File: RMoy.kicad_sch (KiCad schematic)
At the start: 20 parts, among them J1 AudioJack3_SwitchTR, J2 AudioJack3_SwitchTR, J3 Jack-DC, U1 OPA2134

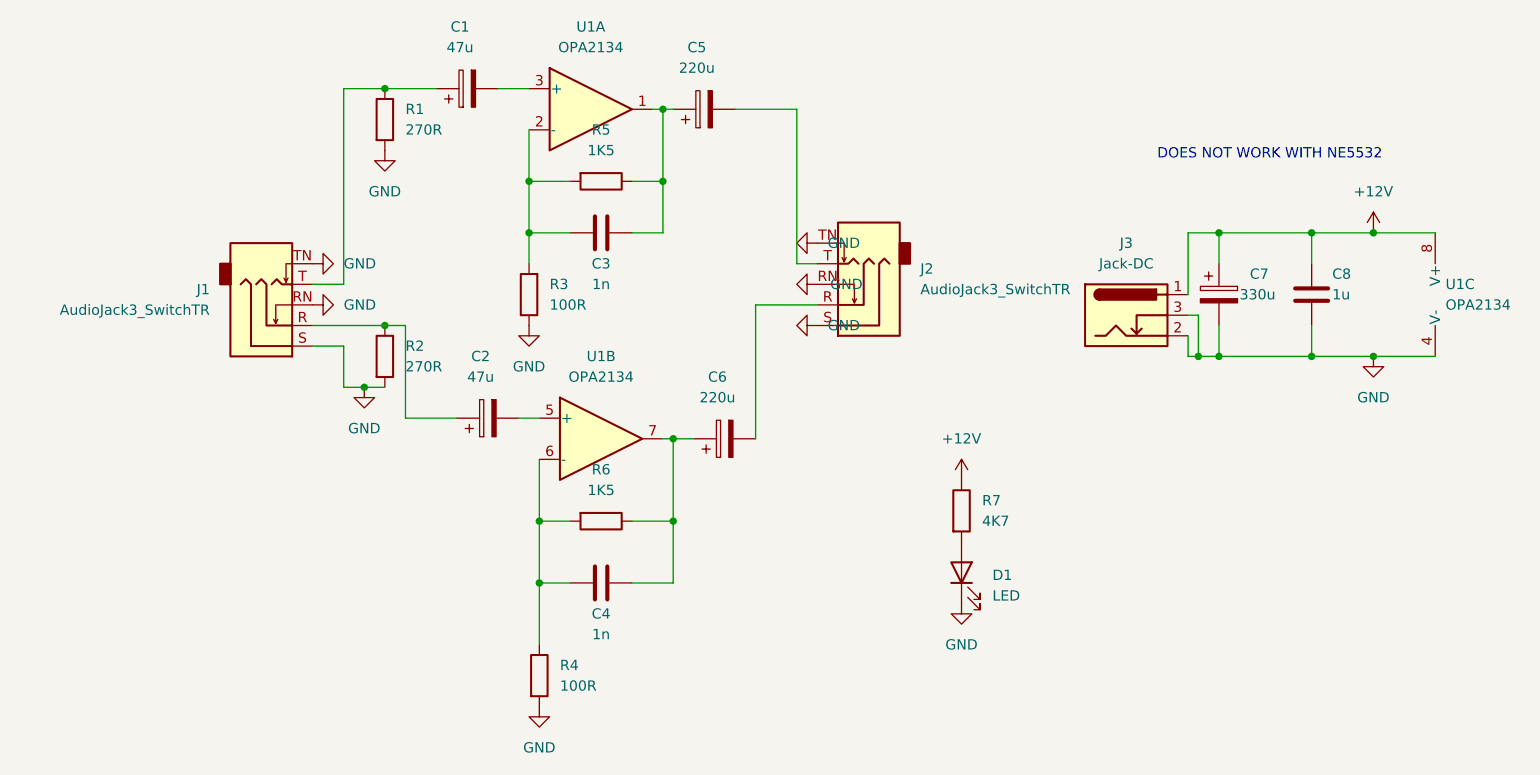
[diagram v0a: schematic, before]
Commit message: add revised parts list
TODO: C1/C2/C5/C6 have not been modified, are they obsolete?
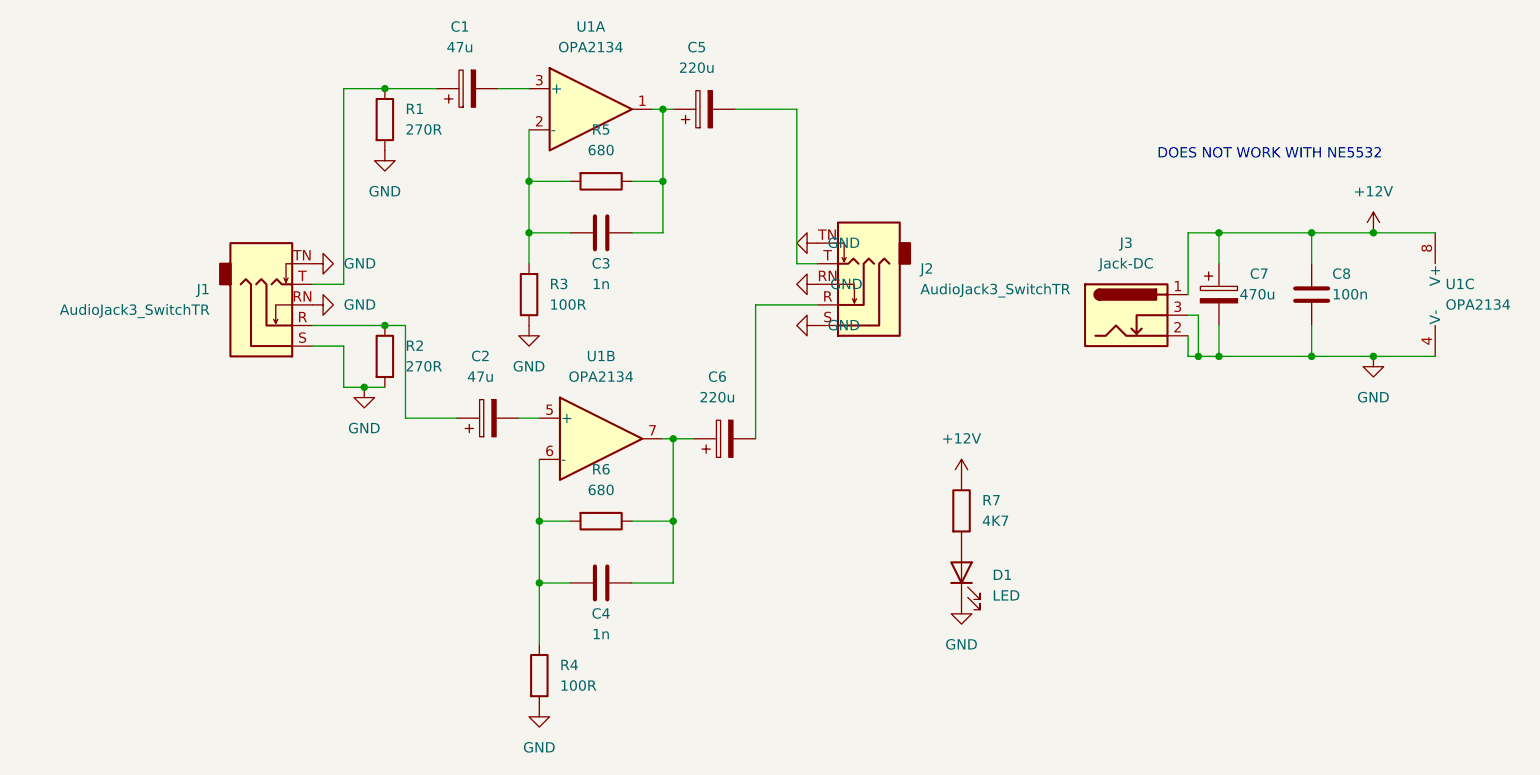
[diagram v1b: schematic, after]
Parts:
- C3, C4: footprint Capacitor_THT:C_Rect_L7.2mm_W2.5mm_P5.00mm_FKS2_FKP2_MKS2_MKP2 -> Capacitor_THT:C_Disc_D5.0mm_W2.5mm_P5.00mm
- C7: value 330u -> 470u
- C8: value 1u -> 100n; footprint Capacitor_THT:C_Rect_L4.6mm_W5.5mm_P2.50mm_MKS02_FKP02 -> Capacitor_THT:C_Disc_D5.0mm_W2.5mm_P5.00mm
- R5, R6: value 1K5 -> 680

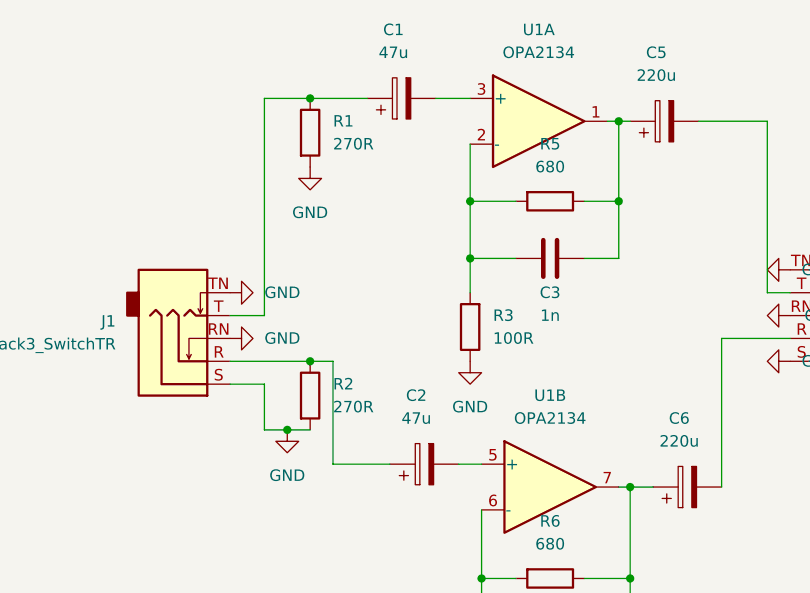
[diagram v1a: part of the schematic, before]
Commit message: C1/C2 are now 100µF non-EOL parts
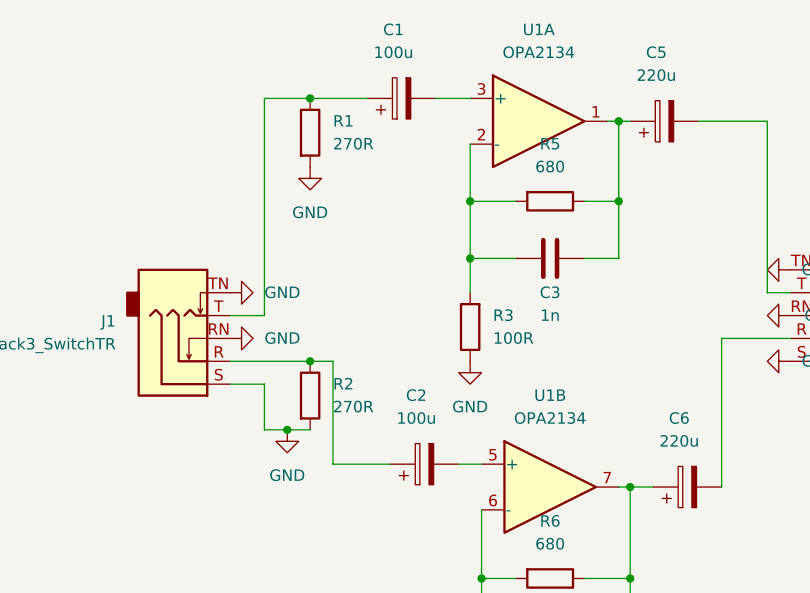
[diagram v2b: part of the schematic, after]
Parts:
- C1, C2: value 47u -> 100u; footprint Capacitor_THT:CP_Radial_D5.0mm_P2.00mm -> Capacitor_THT:CP_Radial_D8.0mm_P3.50mm
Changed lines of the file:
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@@
 			)
 		)
-		(property "Value" "47u"
+		(property "Value" "100u"
 			(at 66.421 67.31 90)
 			(effects
@@
 			)
 		)
-		(property "Footprint" "Capacitor_THT:CP_Radial_D5.0mm_P2.00mm"
+		(property "Footprint" "Capacitor_THT:CP_Radial_D8.0mm_P3.50mm"
 			(at 71.12 71.4248 0)
 			(effects
@@
 			)
 		)
-		(property "Value" "47u"
+		(property "Value" "100u"
 			(at 68.961 107.95 90)
 			(effects
@@
 			)
 		)
-		(property "Footprint" "Capacitor_THT:CP_Radial_D5.0mm_P2.00mm"
+		(property "Footprint" "Capacitor_THT:CP_Radial_D8.0mm_P3.50mm"
 			(at 73.66 112.0648 0)
 			(effects

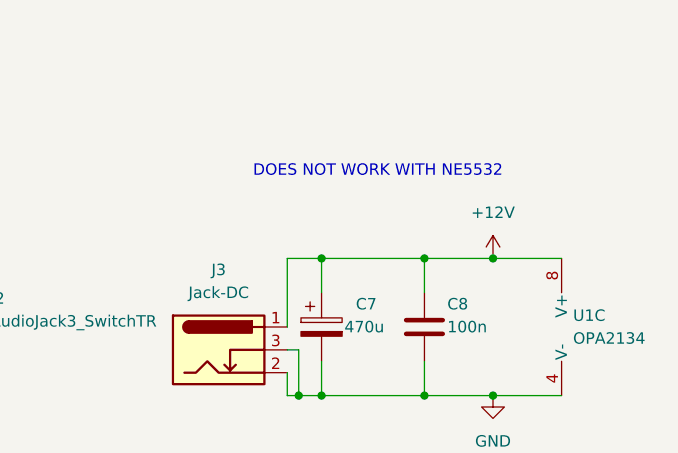
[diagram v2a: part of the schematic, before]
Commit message: PCB is reworked
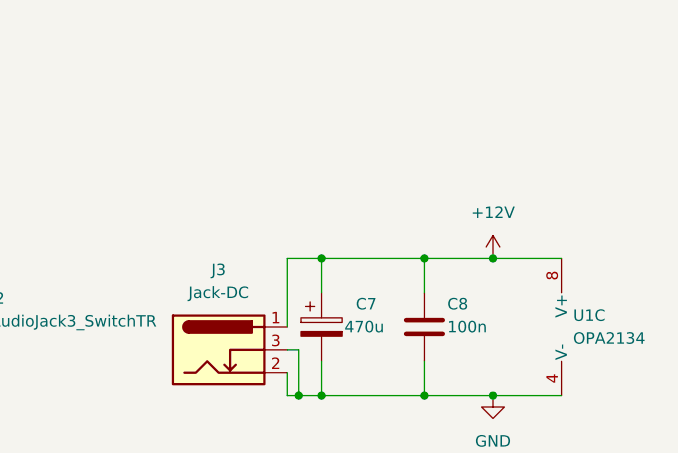
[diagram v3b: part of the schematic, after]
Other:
- note removed: "DOES NOT WORK WITH NE5532"
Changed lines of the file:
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@@
-		)
-	)
-	(text "DOES NOT WORK WITH NE5532"
-		(exclude_from_sim no)
-		(at 152.4 81.28 0)
-		(effects
-			(font
-				(size 1.27 1.27)
-			)
-			(justify left bottom)
 		)
 	)
